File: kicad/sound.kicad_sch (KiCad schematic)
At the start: 17 parts, among them J4 Speaker, U11 74HC02, U16 74HC00, U17 LM386, U3 PSG_AY-3-8912

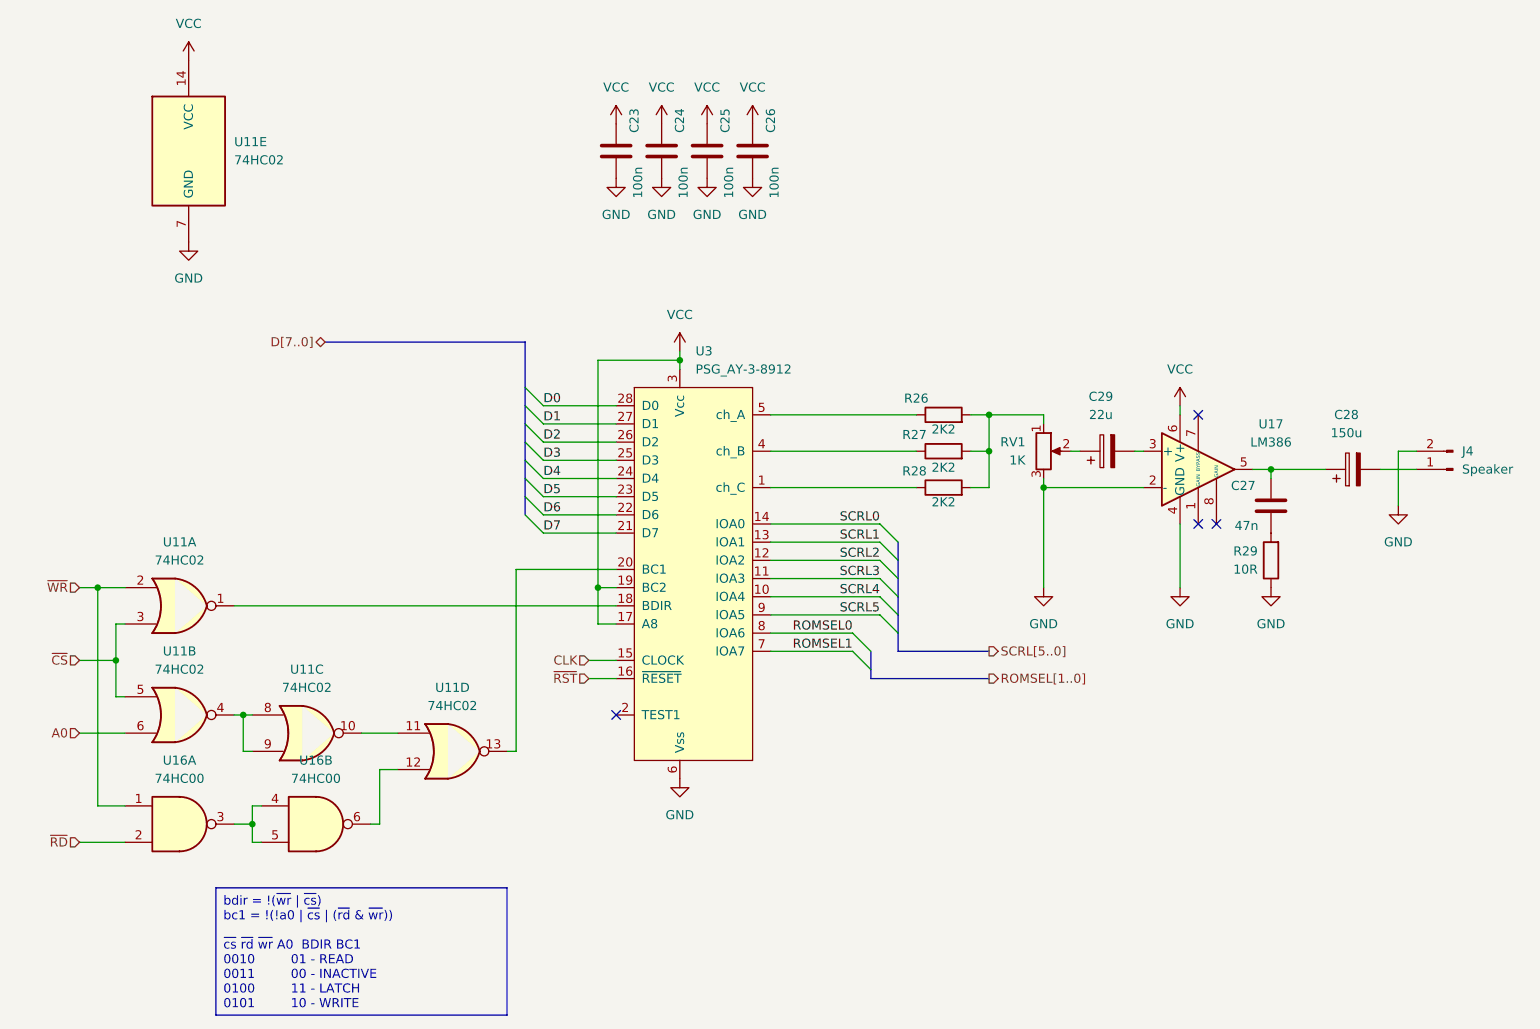
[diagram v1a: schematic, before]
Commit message: HW: Connect 82077 /DREQ to the Z180 DMA ch 1, PCB decorations
Rev B done
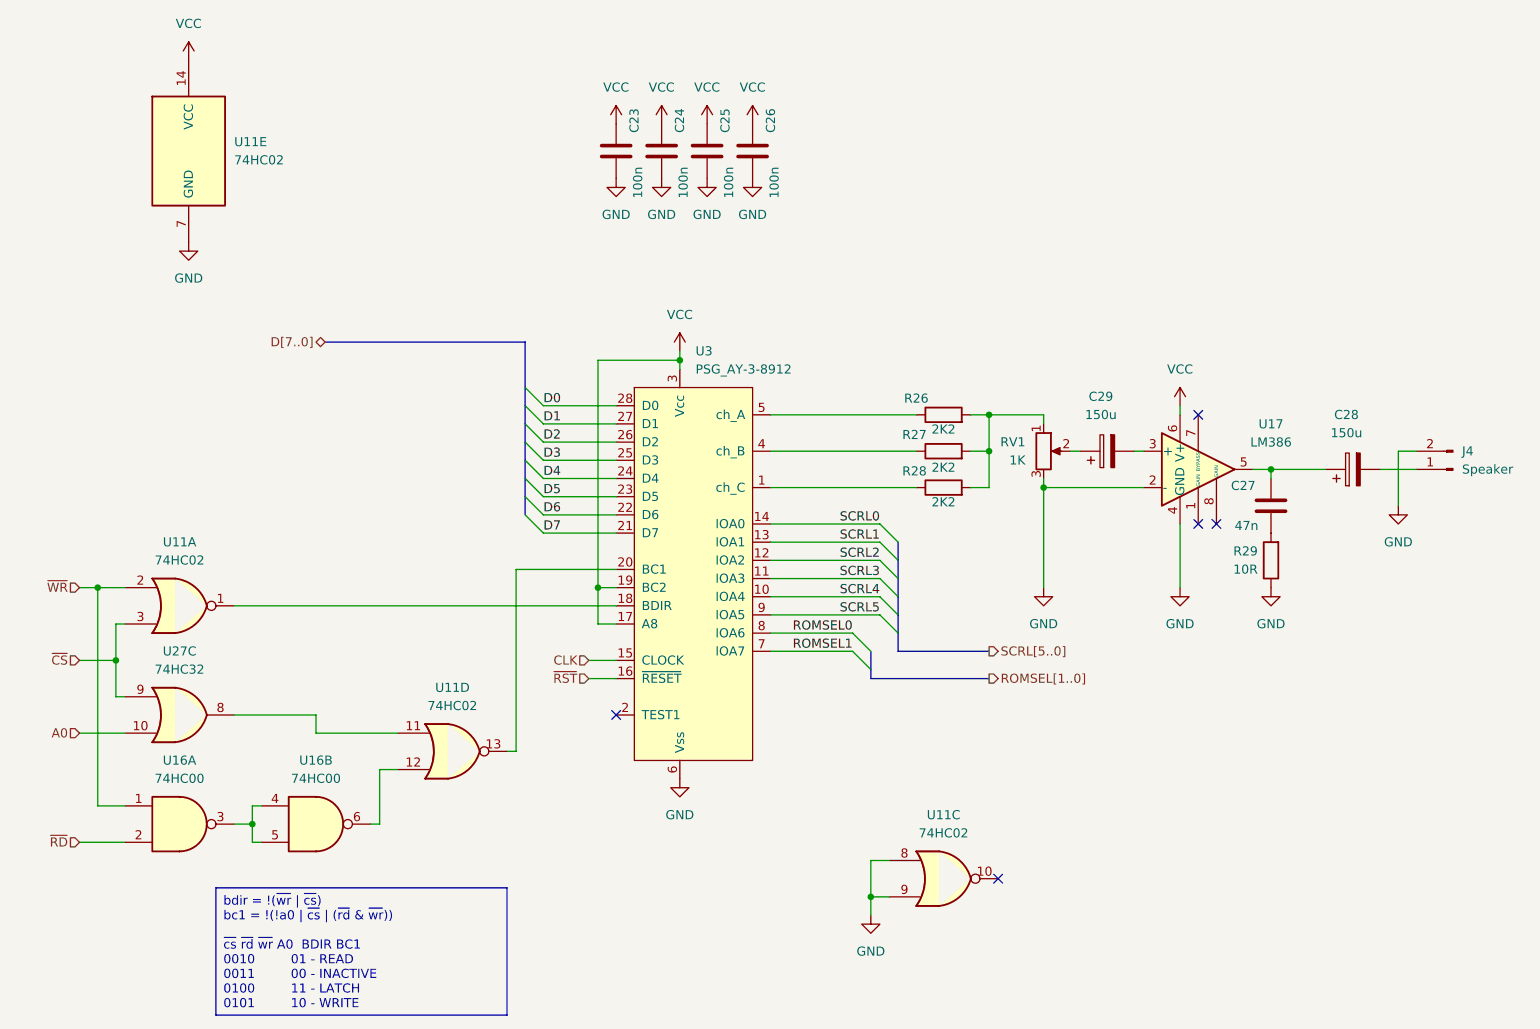
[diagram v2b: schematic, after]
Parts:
- removed unit 2 of U11
- added U27: 74HC32, Package_DIP:DIP-14_W7.62mm, symbol 74xx:74LS32
- C28: footprint Capacitor_THT:CP_Radial_D10.0mm_P5.00mm -> Capacitor_THT:CP_Radial_D6.3mm_P2.50mm
- C29: value 22u -> 150u; footprint Capacitor_THT:CP_Radial_D10.0mm_P5.00mm -> Capacitor_THT:CP_Radial_D6.3mm_P2.50mm
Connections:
- net A0: now also U27.10
- net GND: now also U11.8, U11.9
- net ~{CS}: now also U27.9
- net at U11.11: now also U27.8; no longer U11.10
- no-connect marks 4 -> 5
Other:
- moved on the sheet: U11C
